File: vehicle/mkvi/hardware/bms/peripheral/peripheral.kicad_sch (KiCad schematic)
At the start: 11 parts

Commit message: Add BUILD files and notes to change
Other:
- added sheet Power_Board_M_2_Connection (power_board_connect.kicad_sch)

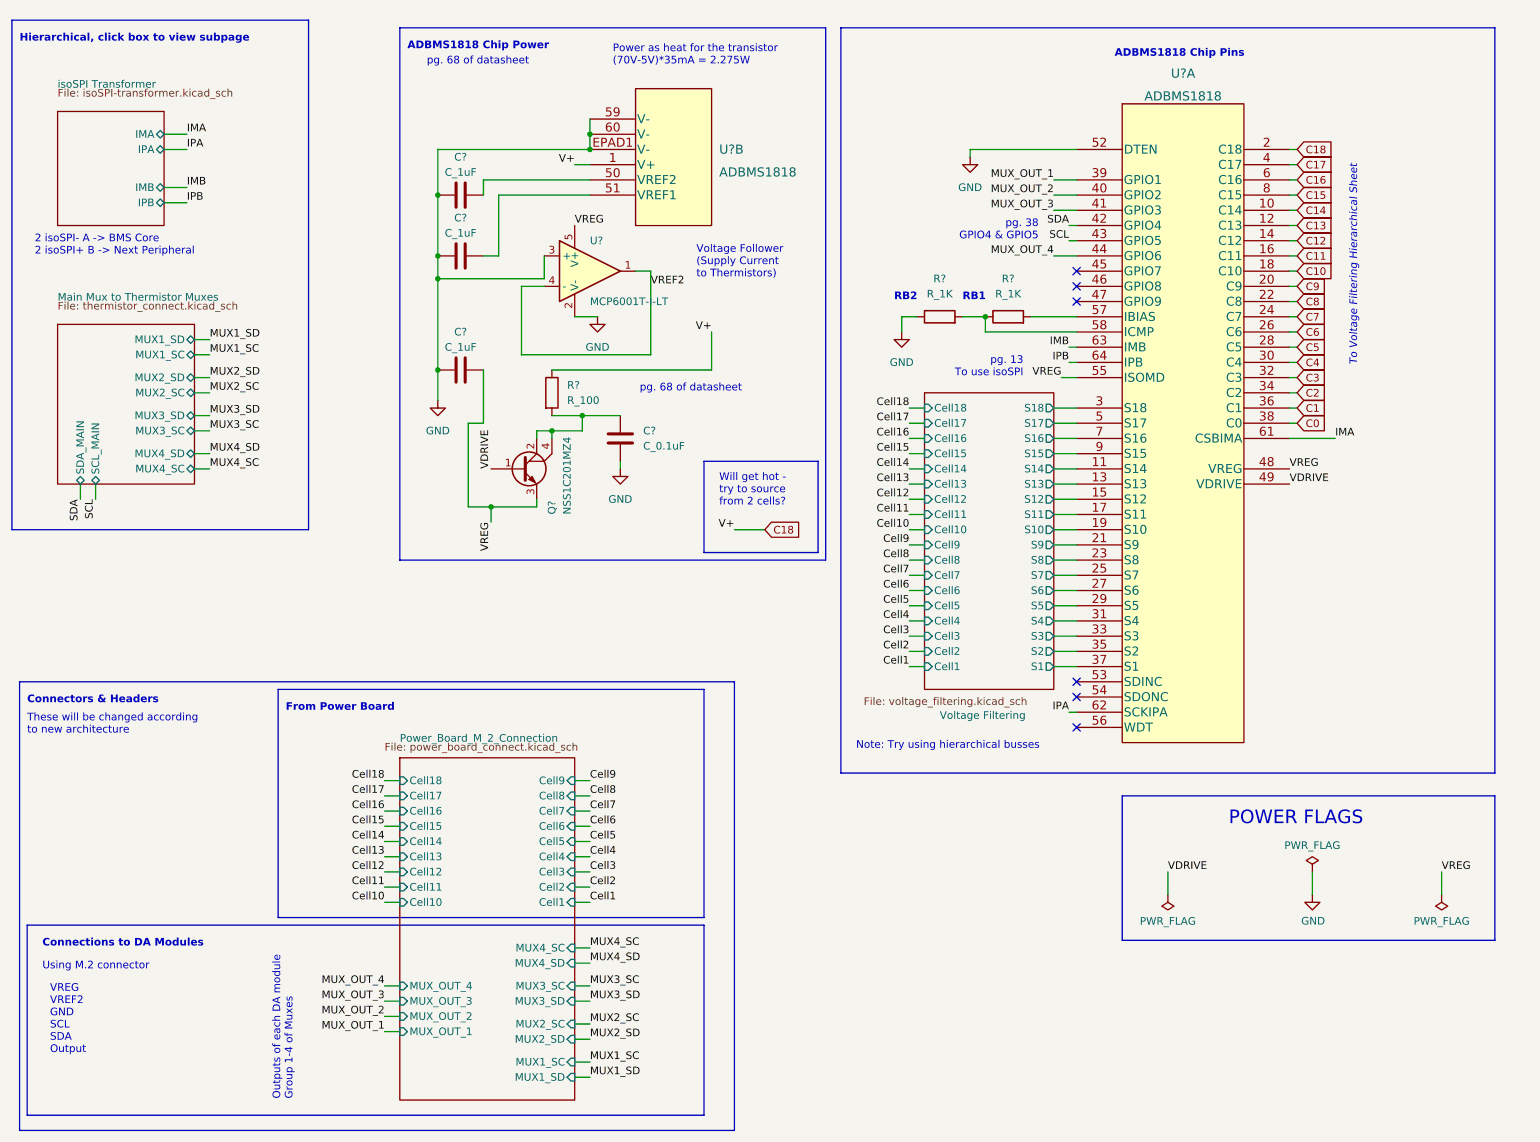
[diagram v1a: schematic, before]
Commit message: Fix transformer symbol and power flags
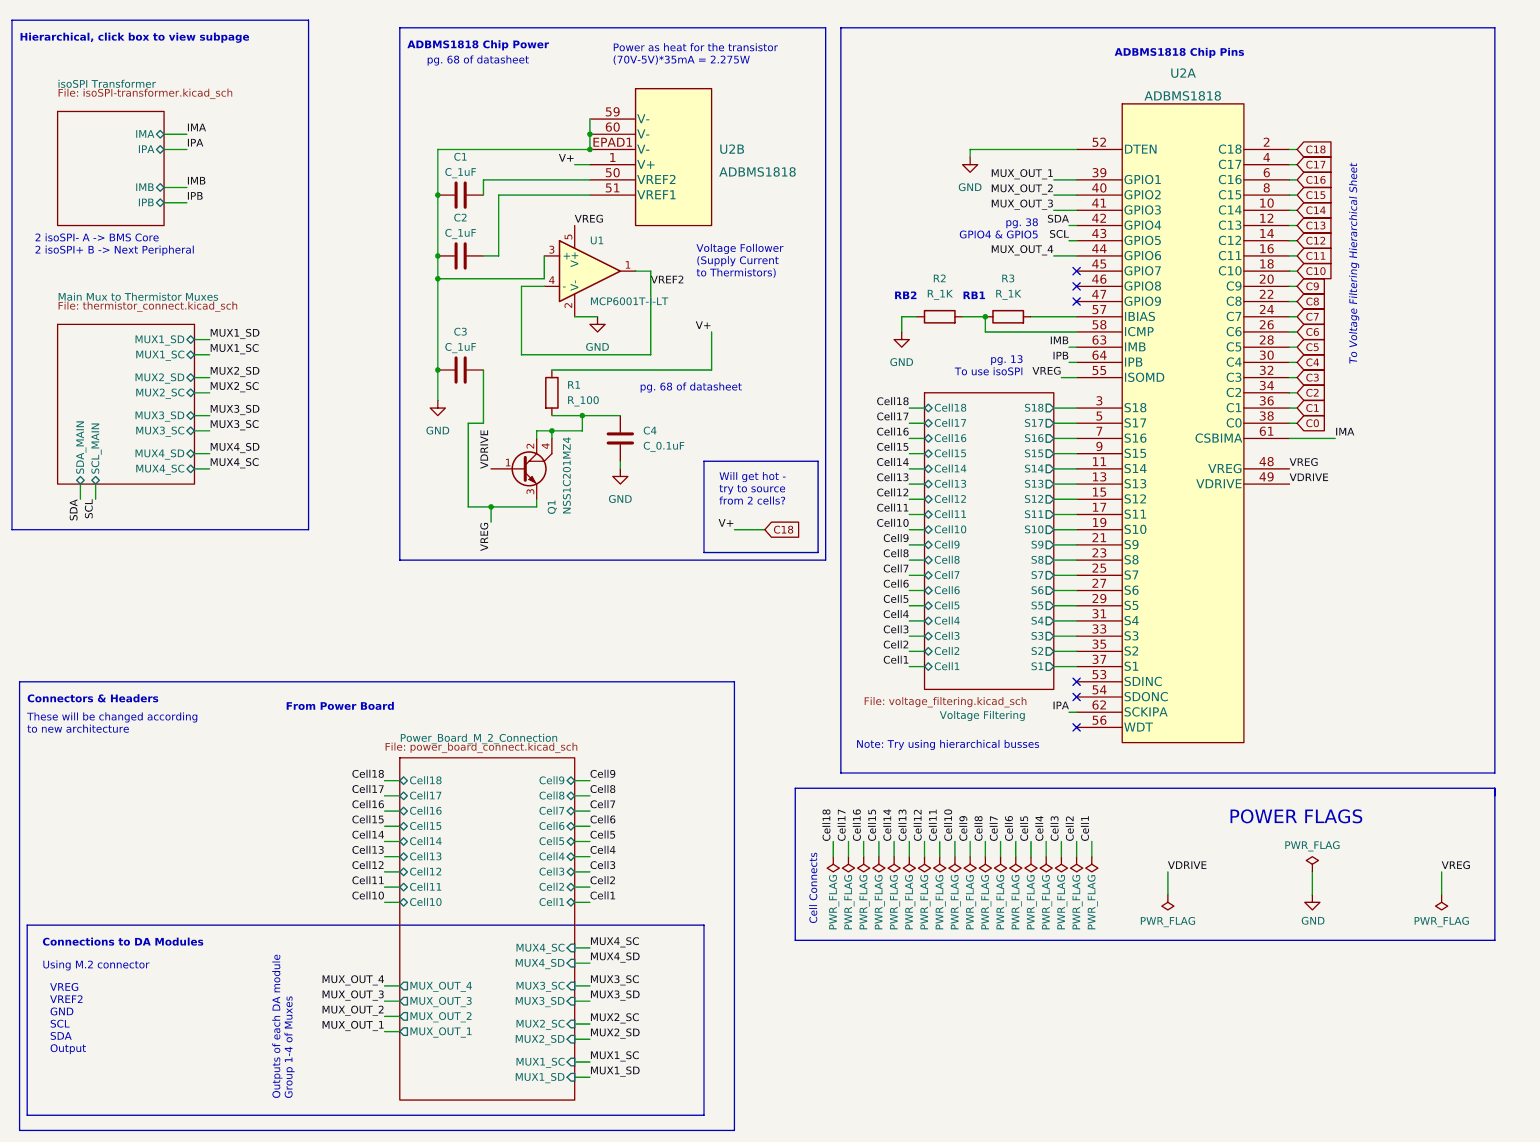
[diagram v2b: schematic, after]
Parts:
- gave numbers to parts that had none: 10
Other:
- note added: "Cell Connects"

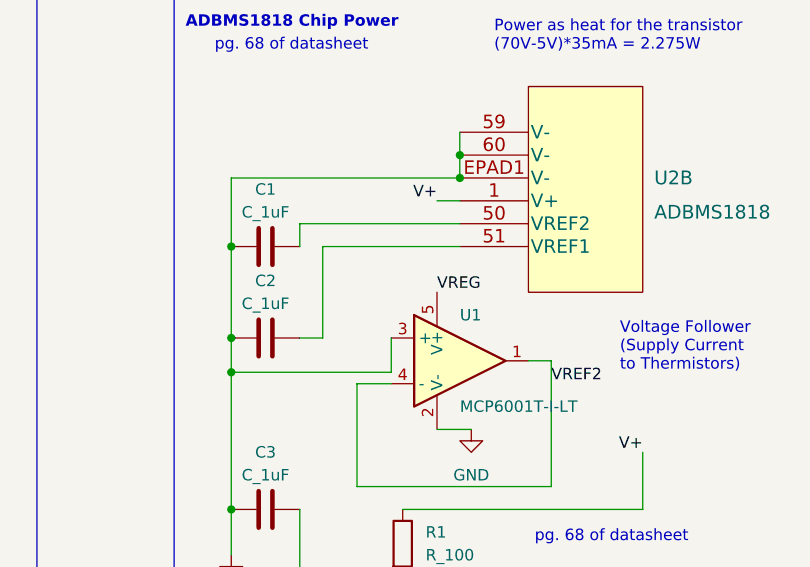
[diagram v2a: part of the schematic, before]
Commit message: M2 connects and new transformer on core
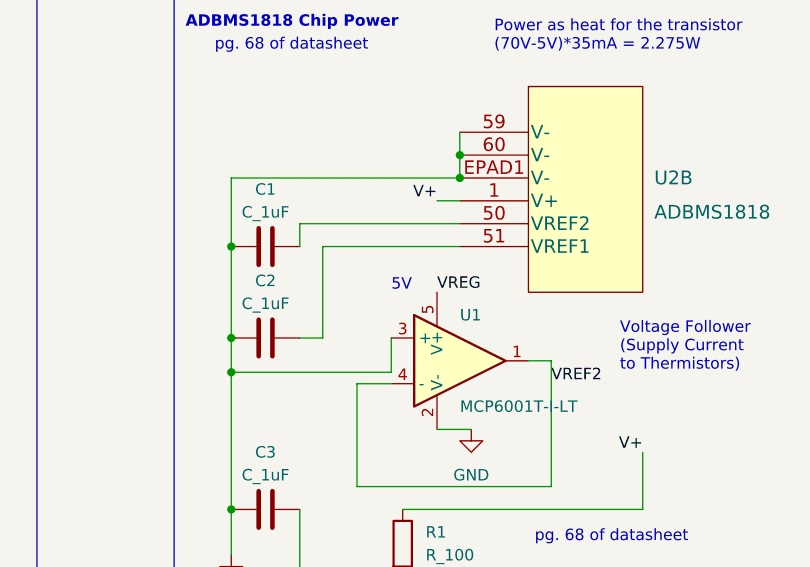
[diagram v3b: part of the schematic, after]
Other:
- note added: "5V"
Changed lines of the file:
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@@
     (effects (font (size 1.27 1.27)) (justify right bottom))
+  )
+  (text "5V" (at 104.14 49.53 0)
+    (effects (font (size 1.27 1.27)) (justify left bottom))
   )
   (text "From Power Board" (at 60.96 130.81 0)
@@
       (reference "#PWR?") (unit 1) (value "GND") (footprint "")
     )
-    (path "/d127e34d-aed7-432d-bc05-2a0055913879/5906c81b-d04d-4638-b157-bdf572cf204f"
+    (path "/d127e34d-aed7-432d-bc05-2a0055913879/5646b193-9269-49dc-9032-ffb6fdb18dbf"
       (reference "#PWR?") (unit 1) (value "GND") (footprint "")
     )
+    (path "/54080254-fdcf-479c-995e-4d4dcf6ca4f0/ebb85c81-0398-431b-a5dc-0d14eb4e20f6"
+      (reference "#PWR?") (unit 1) (value "GND") (footprint "")
+    )

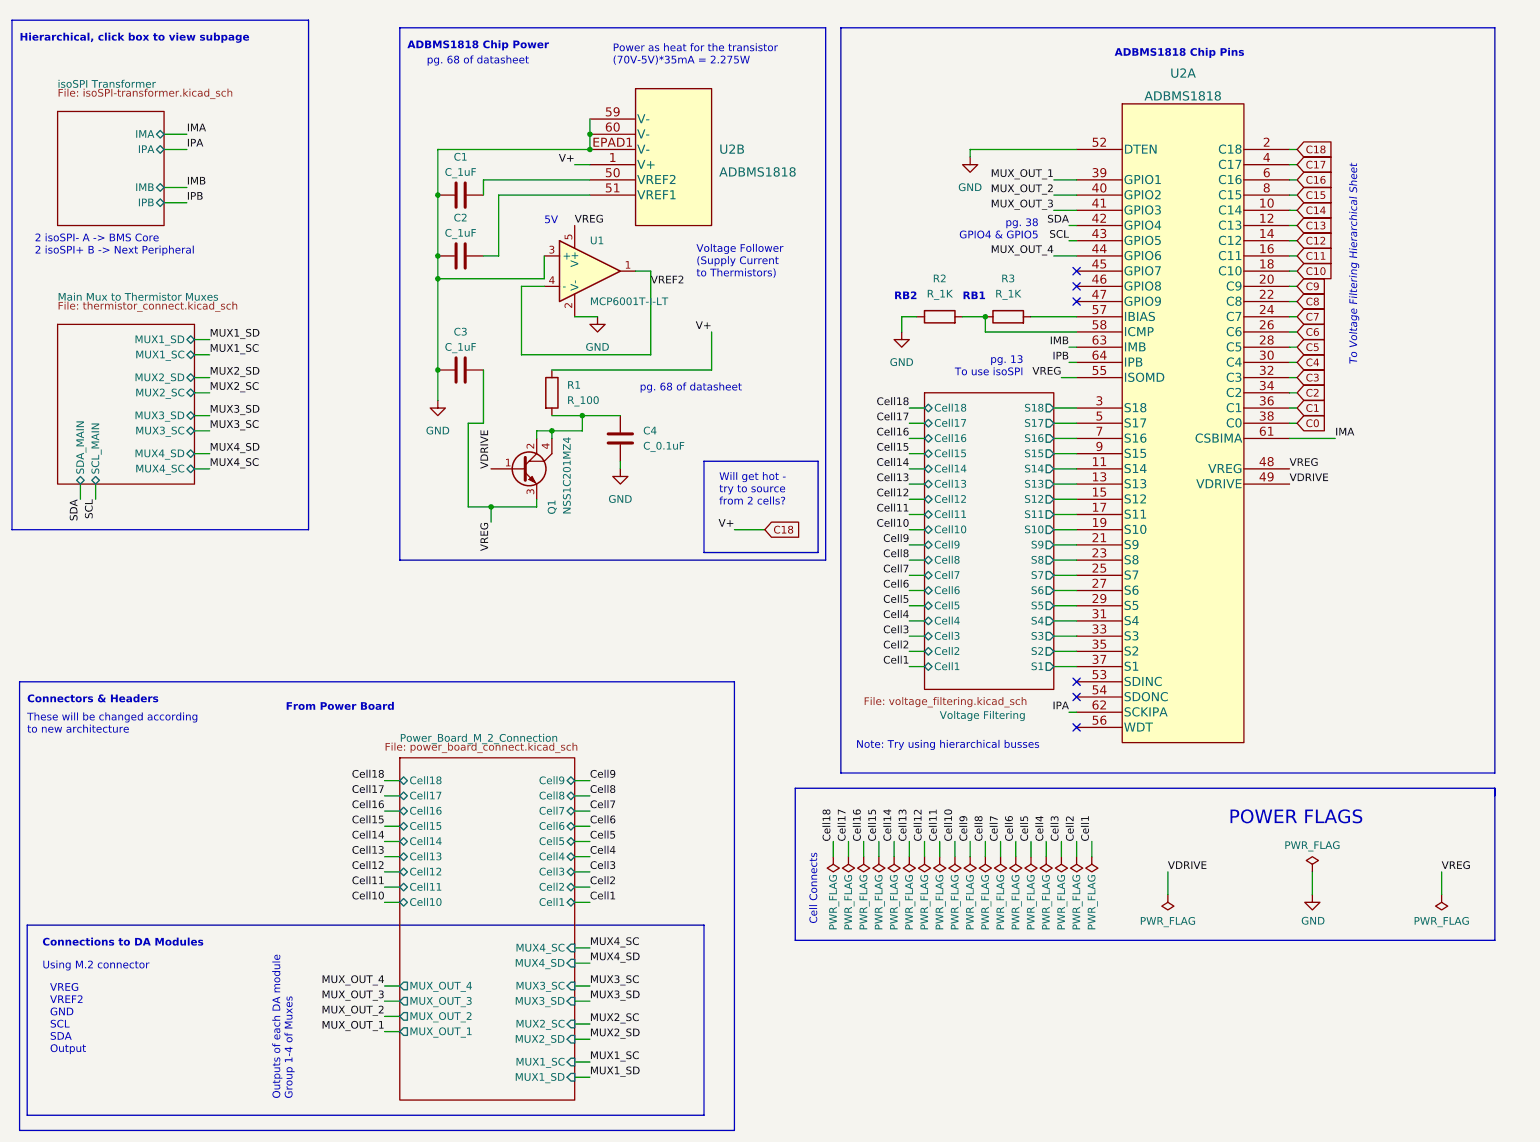
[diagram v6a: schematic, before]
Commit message: M2 connector pins, relay note on BMS core
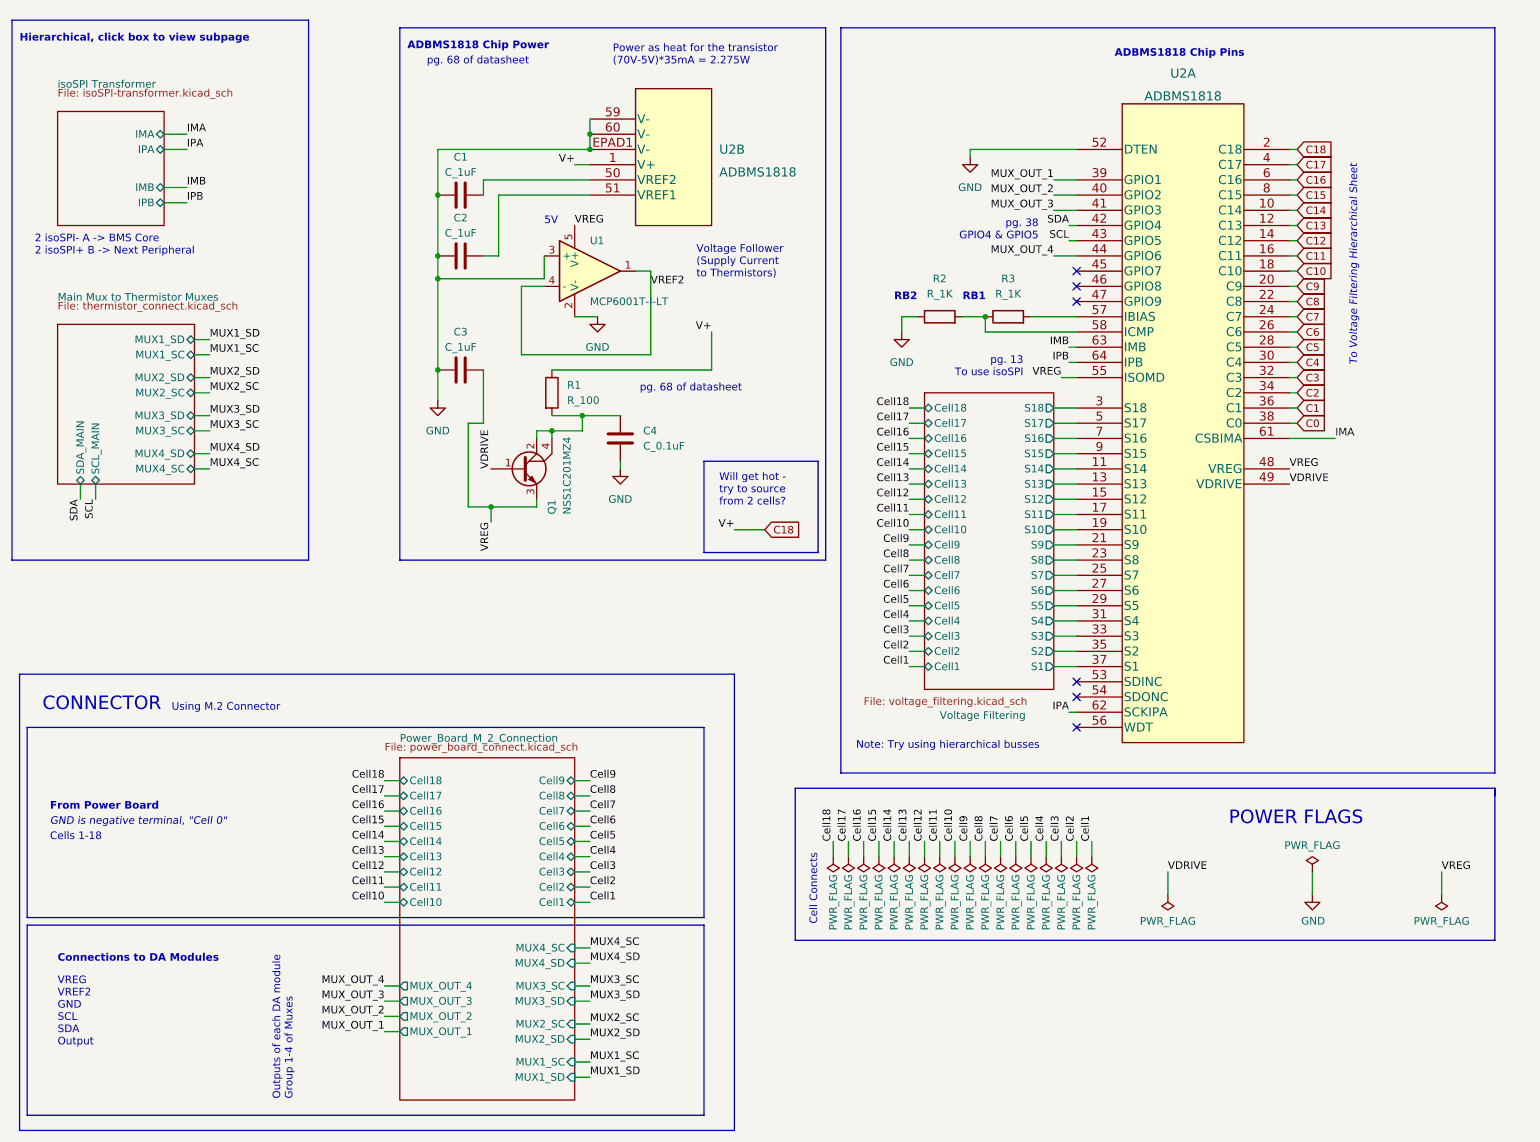
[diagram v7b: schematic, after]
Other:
- note added: "CONNECTOR"
- note added: "Cells 1-18"
- note added: "GND is negative terminal, "Cell 0""
- note added: "Using M.2 Connector"
- note removed: "Connectors & Headers"
- note removed: "These will be changed according to new architecture"
- note removed: "Using M.2 connector"
